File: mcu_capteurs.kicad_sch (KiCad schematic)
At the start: 70 parts, among them J4 STLINK, SW1 435431019840, U2 TCA9517DR, U3 WSEN-PDUS, U4 STM32G474CEUx, Y1 16 MHz

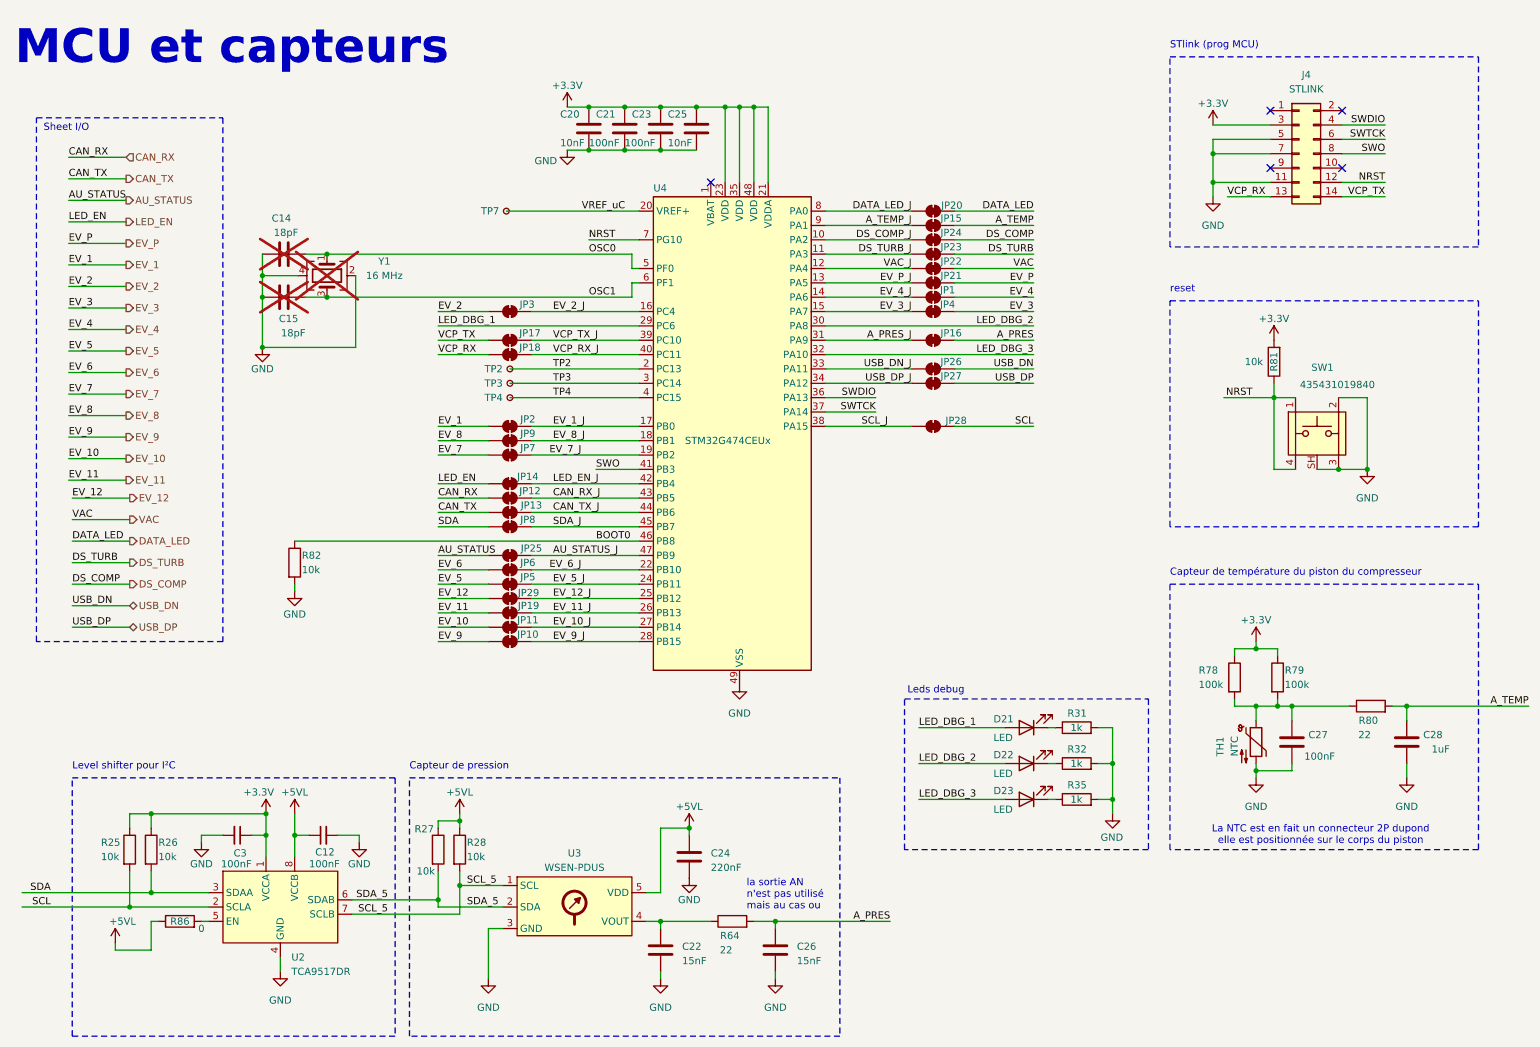
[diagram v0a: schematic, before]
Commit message: nettoyage dossier et assignation de ref JLCPCB
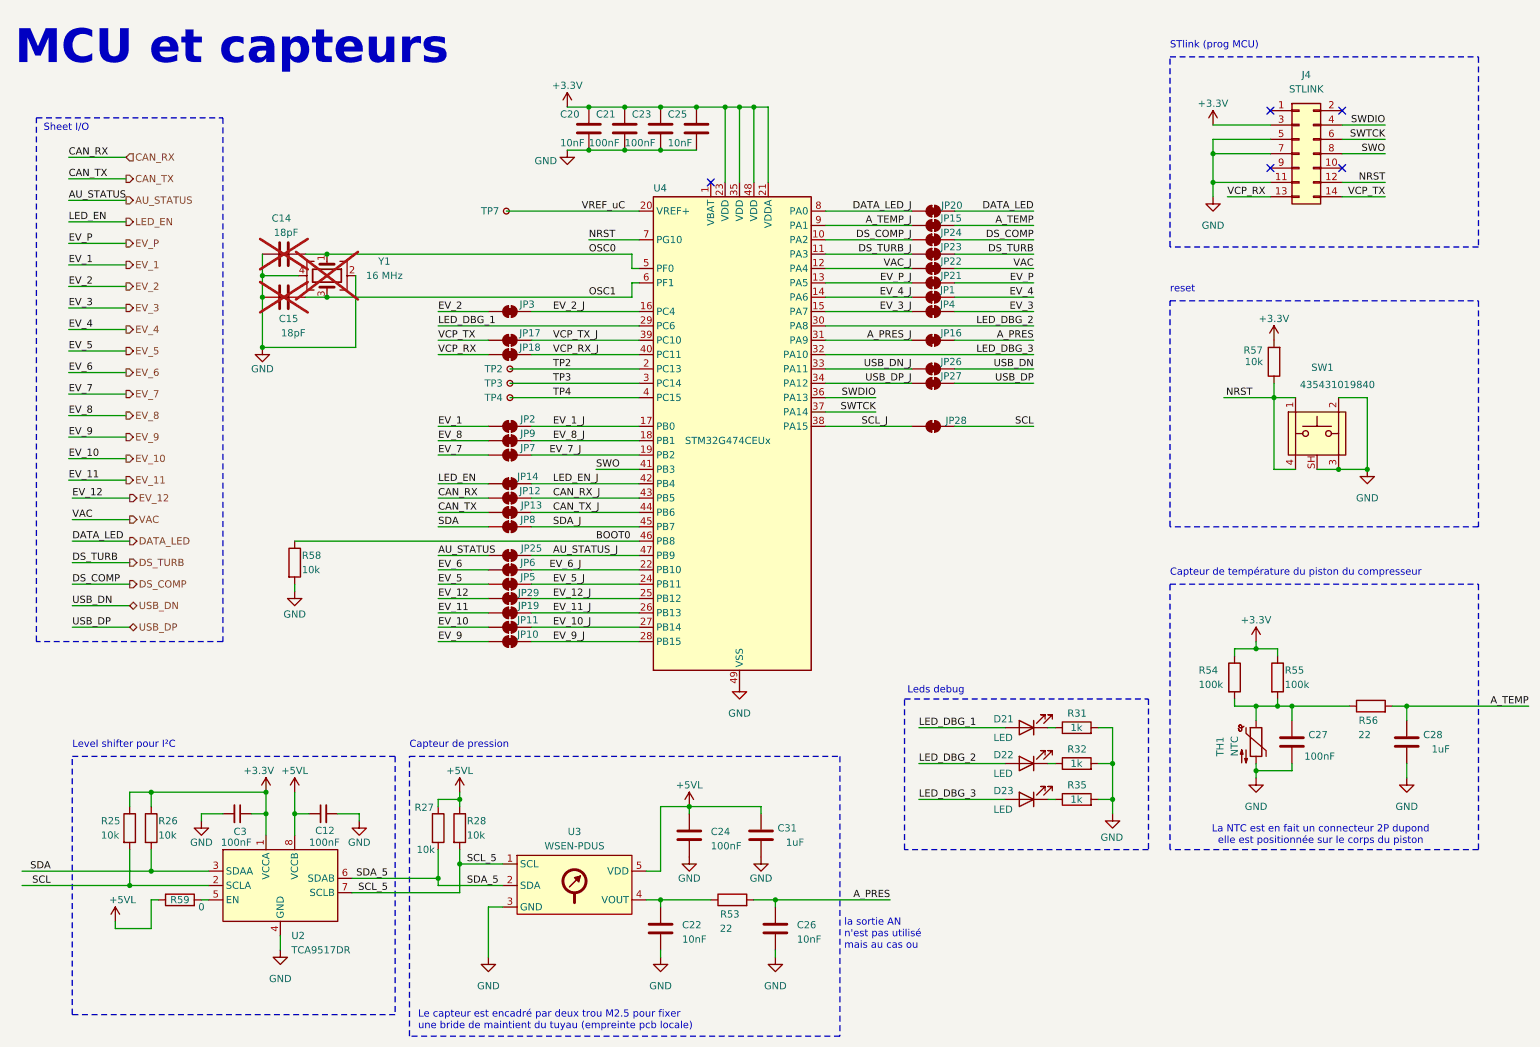
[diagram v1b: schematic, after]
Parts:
- added C31: 1uF, Capacitor_SMD:C_0805_2012Metric, symbol Device:C
- C22, C26: value 15nF -> 10nF
- C24: value 220nF -> 100nF
- TP2, TP3, TP4, TP7: now left out of the parts list
- renumbered R64 to R53, R78 to R54, R79 to R55, R80 to R56, R81 to R57, R82 to R58, R86 to R59
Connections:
- net +5VL: now also C31.2
- net GND: now also C31.1
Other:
- note added: "Le capteur est encadré par deux trou M2.5 pour fixer une bride de maintient du tuyau (empreinte pcb locale)"
- moved on the sheet: C12, C22, C24, C26, C3, R25, R26, R27, R28, R53, R59, U2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

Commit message: Correction orientation conn alim
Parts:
- C12, C21, C23, C24, C27, C3: LCSC (none) -> C14663
- C14, C15: LCSC (none) -> C1647
- C20: LCSC (none) -> C57112; Note (none) -> Découplage
- C22, C26: LCSC (none) -> C57112
- C25: LCSC (none) -> C57112; Max voltage (none) -> 50V
- C28, C31: LCSC (none) -> C28323
- D21: LCSC (none) -> C2286
- D22, D23: LCSC (none) -> C2290
- R25, R26, R27, R28, R57, R58: LCSC (none) -> C25804
- R31, R32, R35: LCSC (none) -> C21190
- R53, R56: LCSC (none) -> C23345
- R54, R55: LCSC (none) -> C25803
- U2: LCSC (none) -> C182421
- U4: LCSC (none) -> C1235412

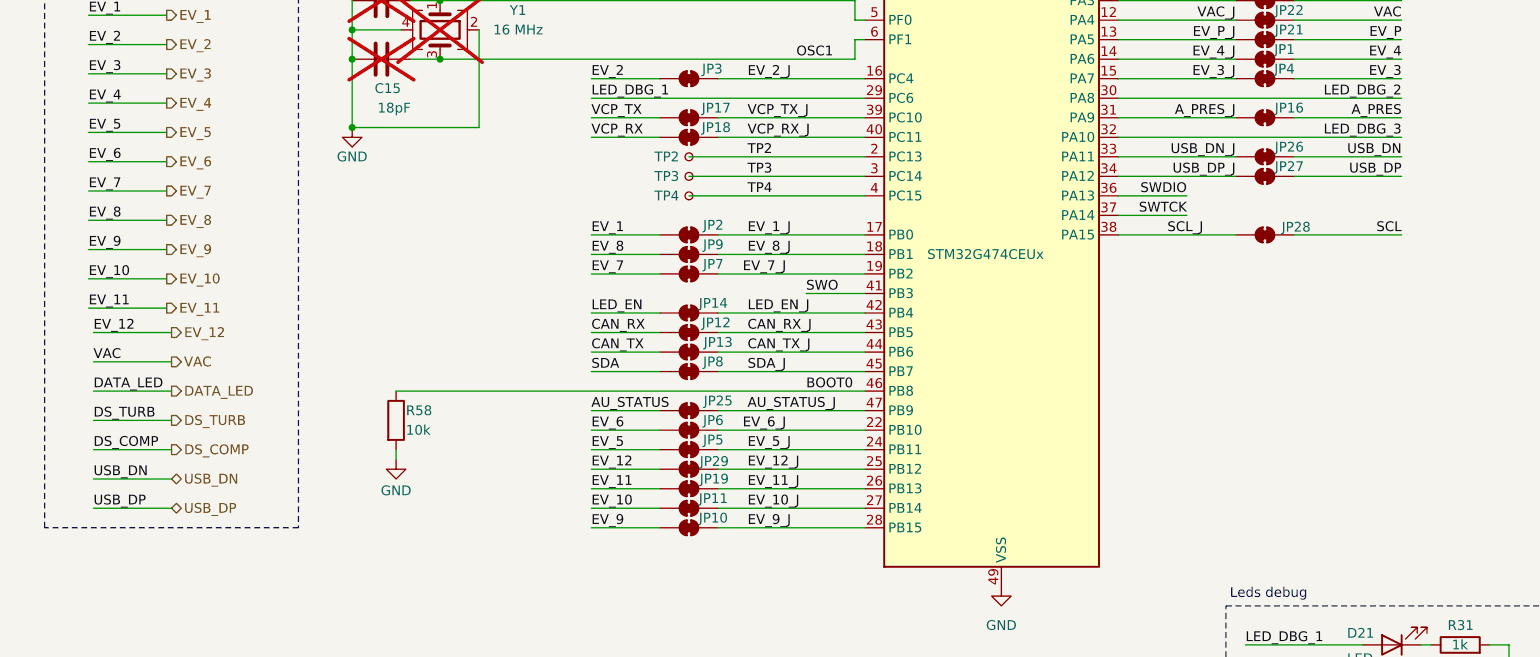
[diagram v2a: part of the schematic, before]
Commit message: debut du tracee des pistes (et modification de l'empreinte R_0402_1005Metric_jumperClosed.kicad_mod pour que le DRC accepte de la router
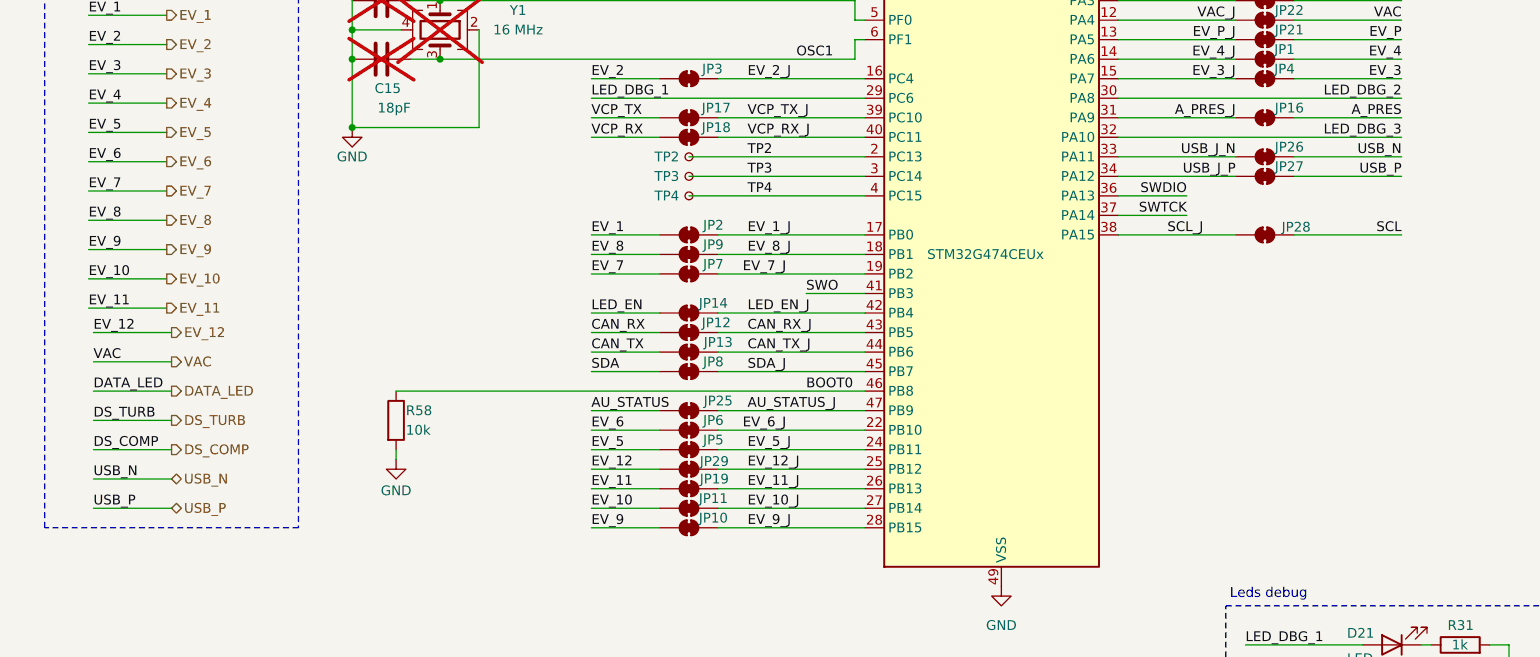
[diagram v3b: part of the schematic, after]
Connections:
- net USB_DN renamed USB_N
- net USB_DN_J renamed USB_J_N
- net USB_DP renamed USB_P
- net USB_DP_J renamed USB_J_P
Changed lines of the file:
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@@
 		)
 	)
-	(label "USB_DN"
+	(label "USB_N"
 		(at 194.31 76.2 180)
 		(effects
@@
 		)
 	)
-	(label "USB_DN"
+	(label "USB_N"
 		(at 24.13 118.11 0)
 		(effects
@@
 		)
 	)
-	(label "USB_DP"
+	(label "USB_P"
 		(at 194.31 78.74 180)
 		(effects
@@
 		)
 	)
-	(label "USB_DP"
+	(label "USB_P"
 		(at 24.13 121.92 0)
 		(effects
@@
 		)
 	)
-	(label "USB_DN_J"
+	(label "USB_J_N"
 		(at 172.72 76.2 180)
 		(effects
@@
 		)
 	)
-	(label "USB_DP_J"
+	(label "USB_J_P"
 		(at 172.72 78.74 180)
 		(effects
@@
 		)
 	)
-	(hierarchical_label "USB_DP"
+	(hierarchical_label "USB_P"
 		(shape bidirectional)
 		(at 34.29 121.92 0)
@@
 		)
 	)
-	(hierarchical_label "USB_DN"
+	(hierarchical_label "USB_N"
 		(shape bidirectional)
 		(at 34.29 118.11 0)

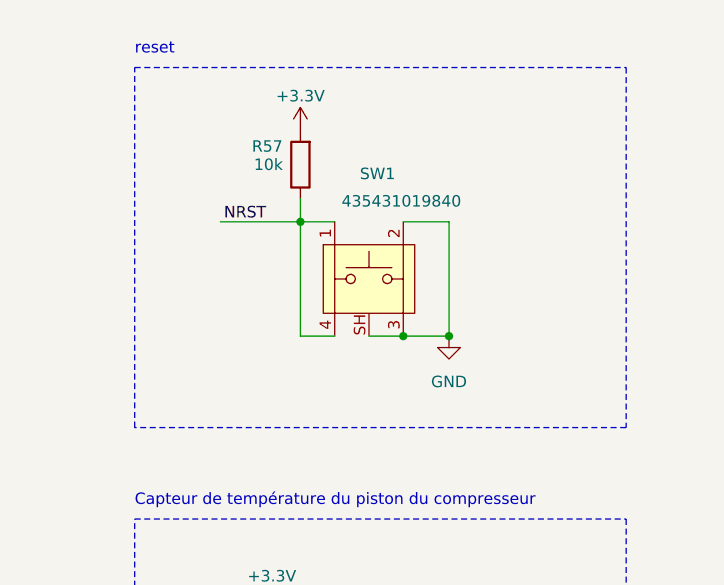
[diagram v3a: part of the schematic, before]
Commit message: added generic JLCPCB switch for reset and gnd netTie
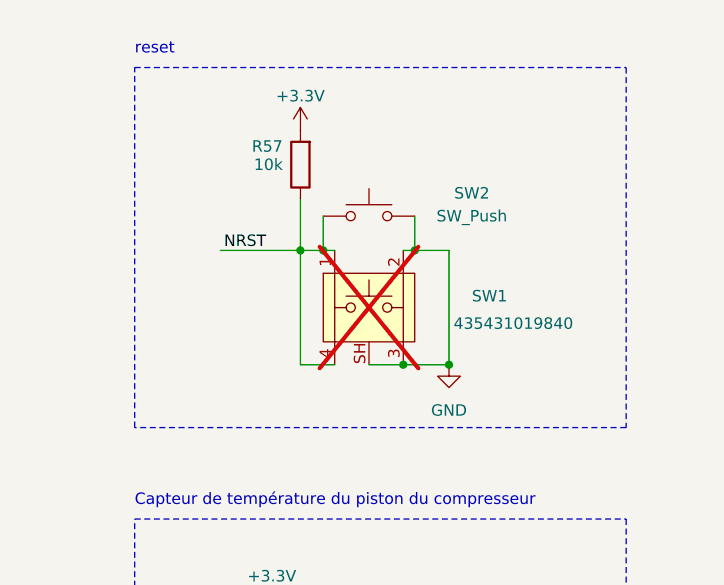
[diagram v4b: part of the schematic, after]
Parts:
- added SW2: SW_Push, Button_Switch_SMD:SW_Push_1P1T_XKB_TS-1187A, symbol Switch:SW_Push
- SW1: now not fitted; now left out of the parts list
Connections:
- net GND: now also SW2.2
- net NRST: now also SW2.1
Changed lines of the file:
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@@
 	)
 	(junction
+		(at 248.285 97.155)
+		(diameter 0)
+		(color 0 0 0 0)
+	)
+	(junction
 		(at 121.92 37.465)
 		(diameter 0)
@@
 	)
 	(junction
-		(at 236.855 81.28)
+		(at 236.855 84.455)
 		(diameter 0)
 		(color 0 0 0 0)
@@
 	)
 	(junction
-		(at 253.365 93.98)
+		(at 253.365 97.155)
 		(diameter 0)
 		(color 0 0 0 0)
@@
 	)
 	(junction
+		(at 239.395 84.455)
+		(diameter 0)
+		(color 0 0 0 0)
+	)
+	(junction
 		(at 260.35 135.89)
 		(diameter 0)
@@
 	)
 	(junction
+		(at 249.555 84.455)
+		(diameter 0)
+		(color 0 0 0 0)
+	)
+	(junction
 		(at 92.71 152.4)
 		(diameter 0)
@@
 		(color 0 0 0 0)
 	)
-	(junction
-		(at 248.285 93.98)
-		(diameter 0)
-		(color 0 0 0 0)
-	)
 	(no_connect
 		(at 137.16 43.18)
@@
 	(wire
 		(pts
-			(xy 240.665 93.98) (xy 236.855 93.98)
+			(xy 240.665 97.155) (xy 236.855 97.155)
 		)
 		(stroke
@@
 	(wire
 		(pts
-			(xy 248.285 93.98) (xy 253.365 93.98)
-		)
-		(stroke
-			(width 0)
-			(type default)
-		)
-	)
-	(wire
-		(pts
 			(xy 233.68 135.89) (xy 237.49 135.89)
 		)
@@
 	(wire
 		(pts
-			(xy 248.285 81.28) (xy 253.365 81.28)
+			(xy 248.285 84.455) (xy 249.555 84.455)
 		)
 		(stroke
@@
 	(wire
 		(pts
-			(xy 244.475 93.98) (xy 248.285 93.98)
+			(xy 244.475 97.155) (xy 248.285 97.155)
 		)
 		(stroke
@@
 	(wire
 		(pts
+			(xy 239.395 80.645) (xy 239.395 84.455)
+		)
+		(stroke
+			(width 0)
+			(type default)
+		)
+	)
+	(wire
+		(pts
 			(xy 23.495 88.265) (xy 33.655 88.265)
 		)
@@
 	(wire
 		(pts
-			(xy 236.855 78.74) (xy 236.855 81.28)
+			(xy 236.855 78.74) (xy 236.855 84.455)
 		)
 		(stroke
@@
 	(wire
 		(pts
+			(xy 239.395 84.455) (xy 240.665 84.455)
+		)
+		(stroke
+			(width 0)
+			(type default)
+		)
+	)
+	(wire
+		(pts
 			(xy 34.29 167.64) (xy 48.26 167.64)
 		)
@@
 	(wire
 		(pts
-			(xy 236.855 81.28) (xy 240.665 81.28)
+			(xy 236.855 84.455) (xy 239.395 84.455)
 		)
 		(stroke
@@
 	(wire
 		(pts
-			(xy 236.855 93.98) (xy 236.855 81.28)
+			(xy 236.855 97.155) (xy 236.855 84.455)
 		)
 		(stroke
@@
 	(wire
 		(pts
-			(xy 253.365 81.28) (xy 253.365 93.98)
+			(xy 253.365 84.455) (xy 253.365 97.155)
 		)
 		(stroke
@@
 	(wire
 		(pts
+			(xy 248.285 97.155) (xy 253.365 97.155)
+		)
+		(stroke
+			(width 0)
+			(type default)
+		)
+	)
+	(wire
+		(pts
 			(xy 63.5 106.68) (xy 124.46 106.68)
 		)
@@
 	(wire
 		(pts
-			(xy 227.965 81.28) (xy 236.855 81.28)
+			(xy 227.965 84.455) (xy 236.855 84.455)
 		)
 		(stroke
@@
 	(wire
 		(pts
+			(xy 249.555 80.645) (xy 249.555 84.455)
+		)
+		(stroke
+			(width 0)
+			(type default)
+		)
+	)
+	(wire
+		(pts
 			(xy 23.495 80.645) (xy 33.655 80.645)
 		)
@@
 	(wire
 		(pts
+			(xy 249.555 84.455) (xy 253.365 84.455)
+		)
+		(stroke
+			(width 0)
+			(type default)
+		)
+	)
+	(wire
+		(pts
 			(xy 116.84 93.98) (xy 124.46 93.98)
 		)
@@
 	)
 	(label "NRST"
-		(at 233.045 81.28 180)
+		(at 233.045 84.455 180)
 		(effects
 			(font
@@
 	)
 	(symbol
+		(lib_id "Switch:SW_Push")
+		(at 244.475 80.645 0)
+		(unit 1)
+		(exclude_from_sim no)
+		(in_bom yes)
+		(on_board yes)
+		(dnp no)
+		(property "Reference" "SW2"
+			(at 255.905 78.105 0)
+			(effects
+				(font
+					(size 1.27 1.27)
+				)
+			)
+		)
+		(property "Value" "SW_Push"
+			(at 255.905 80.645 0)
+			(effects
+				(font
+					(size 1.27 1.27)
+				)
+			)
+		)
+		(property "Footprint" "Button_Switch_SMD:SW_Push_1P1T_XKB_TS-1187A"
+			(at 244.475 75.565 0)
+			(effects
+				(font
+					(size 1.27 1.27)
+				)
+				(hide yes)
+			)
+		)
+		(property "Datasheet" "~"
+			(at 244.475 75.565 0)
+			(effects
+				(font
+					(size 1.27 1.27)
+				)
+				(hide yes)
+			)
+		)
+		(property "Description" "Push button switch, generic, two pins"
+			(at 244.475 80.645 0)
+			(effects
+				(font
+					(size 1.27 1.27)
+				)
+				(hide yes)
+			)
+		)
+		(pin "1"
+		)
+		(pin "2"
+		)
+		(instances
+			(project ""
+				(path "/d0b6cc72-ff07-4f5e-a148-04b65c86a715/f78de832-b1c2-4647-81ab-fdc60f9d045f"
+					(reference "SW2")
+					(unit 1)
+				)
+			)
+		)
+	)
+	(symbol
 		(lib_id "power:GND")
-		(at 253.365 93.98 0)
+		(at 253.365 97.155 0)
 		(unit 1)
 		(exclude_from_sim no)
@@
 		(fields_autoplaced yes)
 		(property "Reference" "#PWR54"
-			(at 253.365 100.33 0)
+			(at 253.365 103.505 0)
 			(effects
 				(font
@@
 		)
 		(property "Value" "GND"
-			(at 253.365 99.06 0)
+			(at 253.365 102.235 0)
 			(effects
 				(font
@@
 		)
 		(property "Footprint" ""
-			(at 253.365 93.98 0)
+			(at 253.365 97.155 0)
 			(effects
 				(font
@@
 		)
 		(property "Datasheet" ""
-			(at 253.365 93.98 0)
+			(at 253.365 97.155 0)
 			(effects
 				(font
@@
 		)
 		(property "Description" ""
-			(at 253.365 93.98 0)
+			(at 253.365 97.155 0)
 			(effects
 				(font
@@
 	(symbol
 		(lib_id "ComponentsEvo:435431019840")
-		(at 244.475 87.63 0)
+		(at 244.475 90.805 0)
 		(unit 1)
 		(exclude_from_sim no)
-		(in_bom yes)
+		(in_bom no)
 		(on_board yes)
-		(dnp no)
+		(dnp yes)
 		(property "Reference" "SW1"
-			(at 243.459 75.946 0)
+			(at 255.905 89.535 0)
 			(effects
 				(font
@@
 		)
 		(property "Value" "435431019840"
-			(at 241.427 78.994 0)
+			(at 253.873 92.583 0)
 			(effects
 				(font
@@
 		)
 		(property "Footprint" "ComponentsEvo:435431019840"
-			(at 244.475 102.87 0)
+			(at 244.475 106.045 0)
 			(effects
 				(font
@@
 		)
 		(property "Datasheet" "https://www.we-online.com/components/products/datasheet/435431019840.pdf"
-			(at 244.475 104.14 0)
+			(at 244.475 107.315 0)
 			(effects
 				(font
@@
 		)
 		(property "Description" "Push button switch, generic, two pins"
-			(at 244.475 87.63 0)
+			(at 244.475 90.805 0)
 			(effects
 				(font

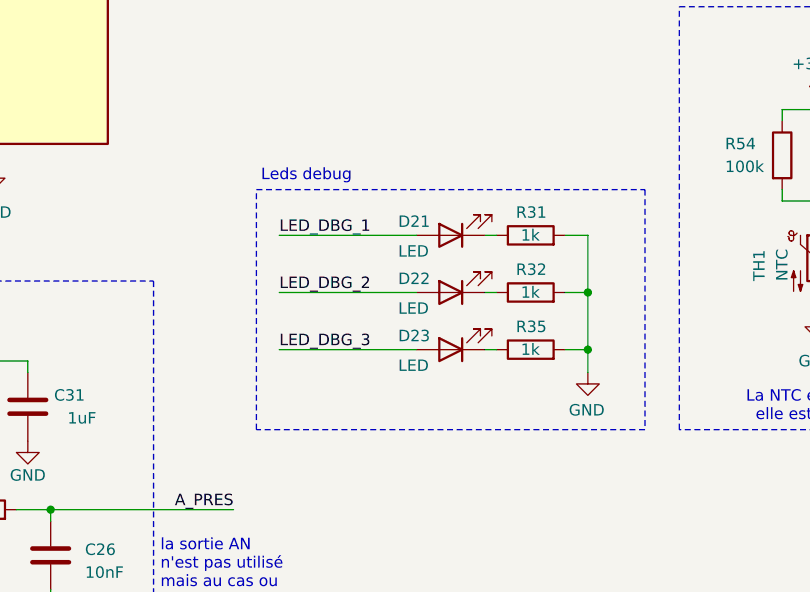
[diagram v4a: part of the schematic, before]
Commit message: corrrection footprint trim, ajout R64, config JLCPCB ASSY, fin panelisation (TODO: revue et cmd)
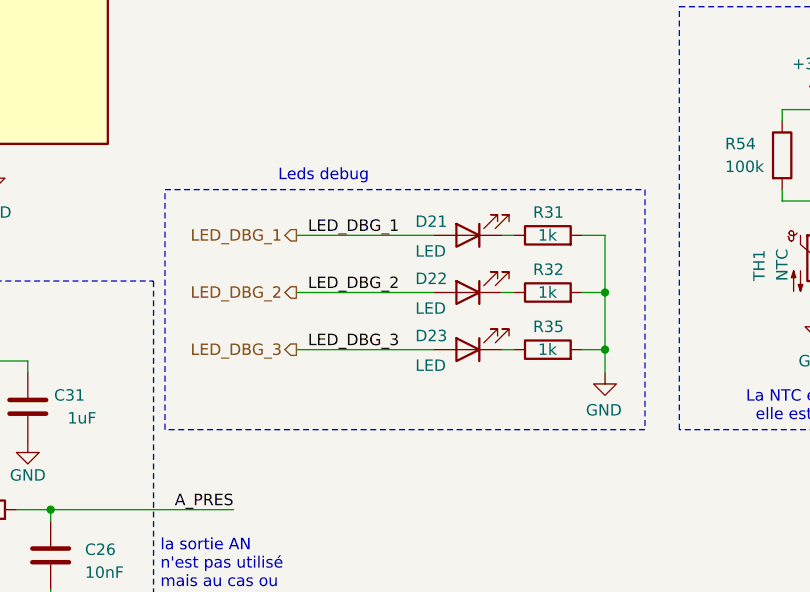
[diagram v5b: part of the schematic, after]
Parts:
- SW2: LCSC (none) -> C318884
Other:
- moved on the sheet: D21, D22, D23, R31, R32, R35
